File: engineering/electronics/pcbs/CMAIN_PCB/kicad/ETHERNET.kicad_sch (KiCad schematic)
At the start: 8 parts, among them J47 GIGABLOX_NANO_SWITCH_REVA_MOD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, J48 SM04B-GHS-TB_LF__SN_, J51 GIGABLOX_NANO_SWITCH_REVA_MOD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, J52 SM04B-GHS-TB_LF__SN_, U13 SMTWEM245STR, U14 SMTWEM245STR, U15 SMTWEM245STR, U16 SMTWEM245STR

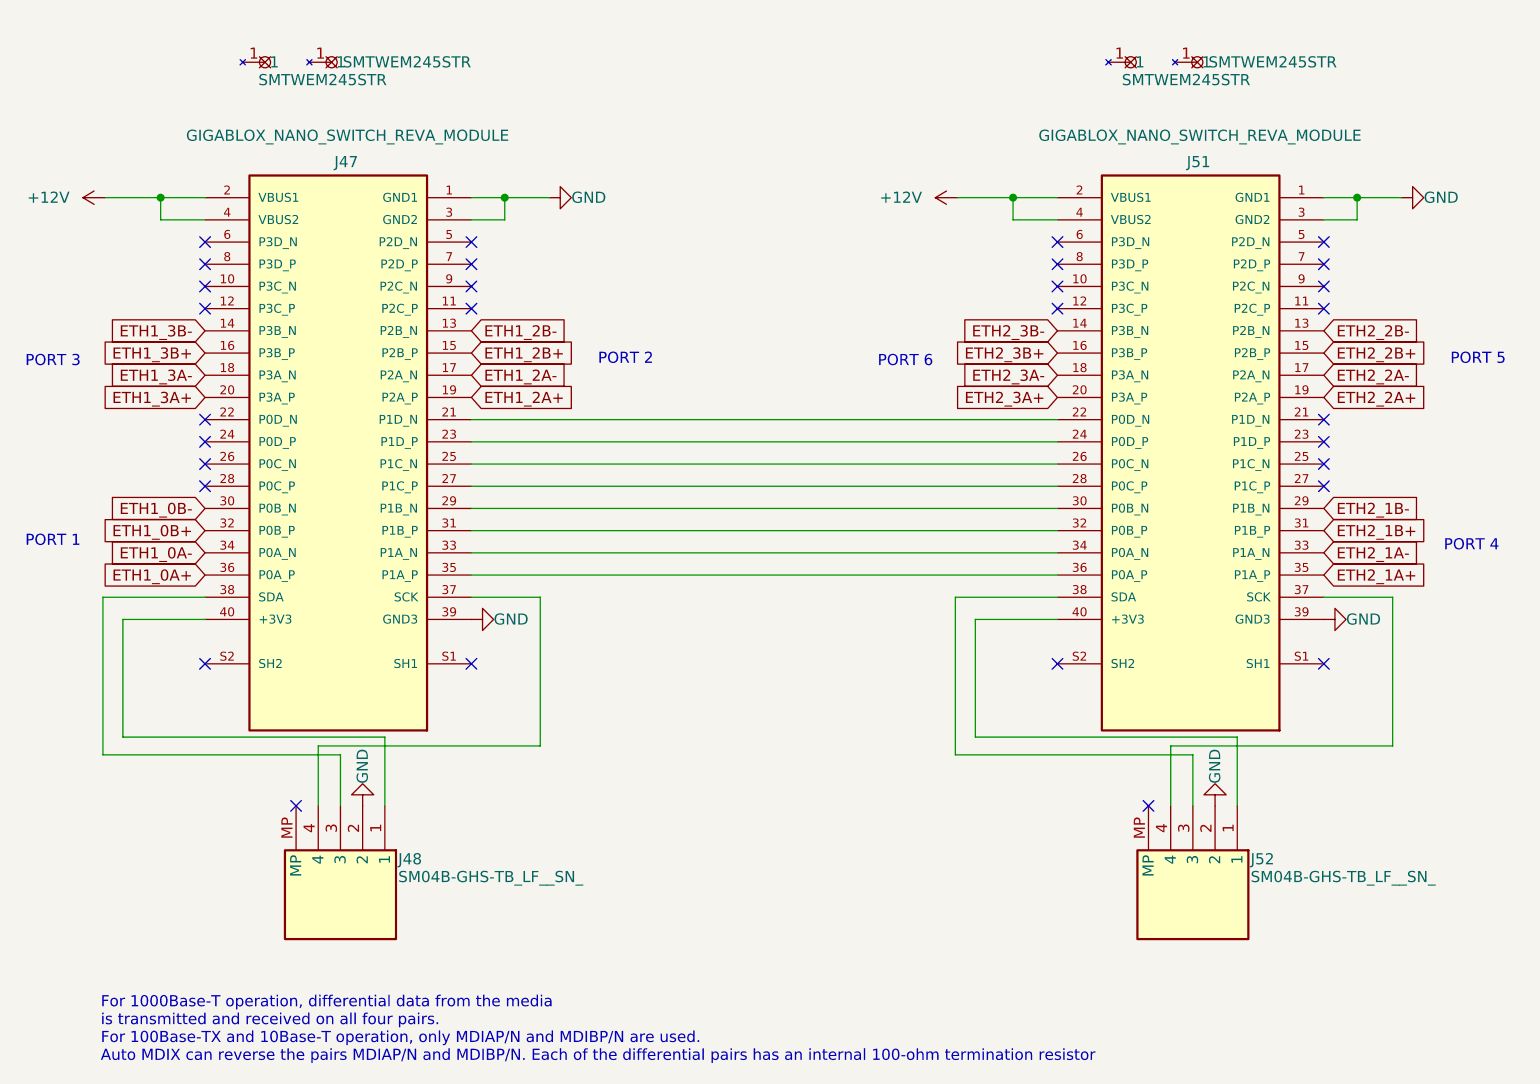
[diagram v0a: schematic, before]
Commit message: Import linked CMAIN PCB layout
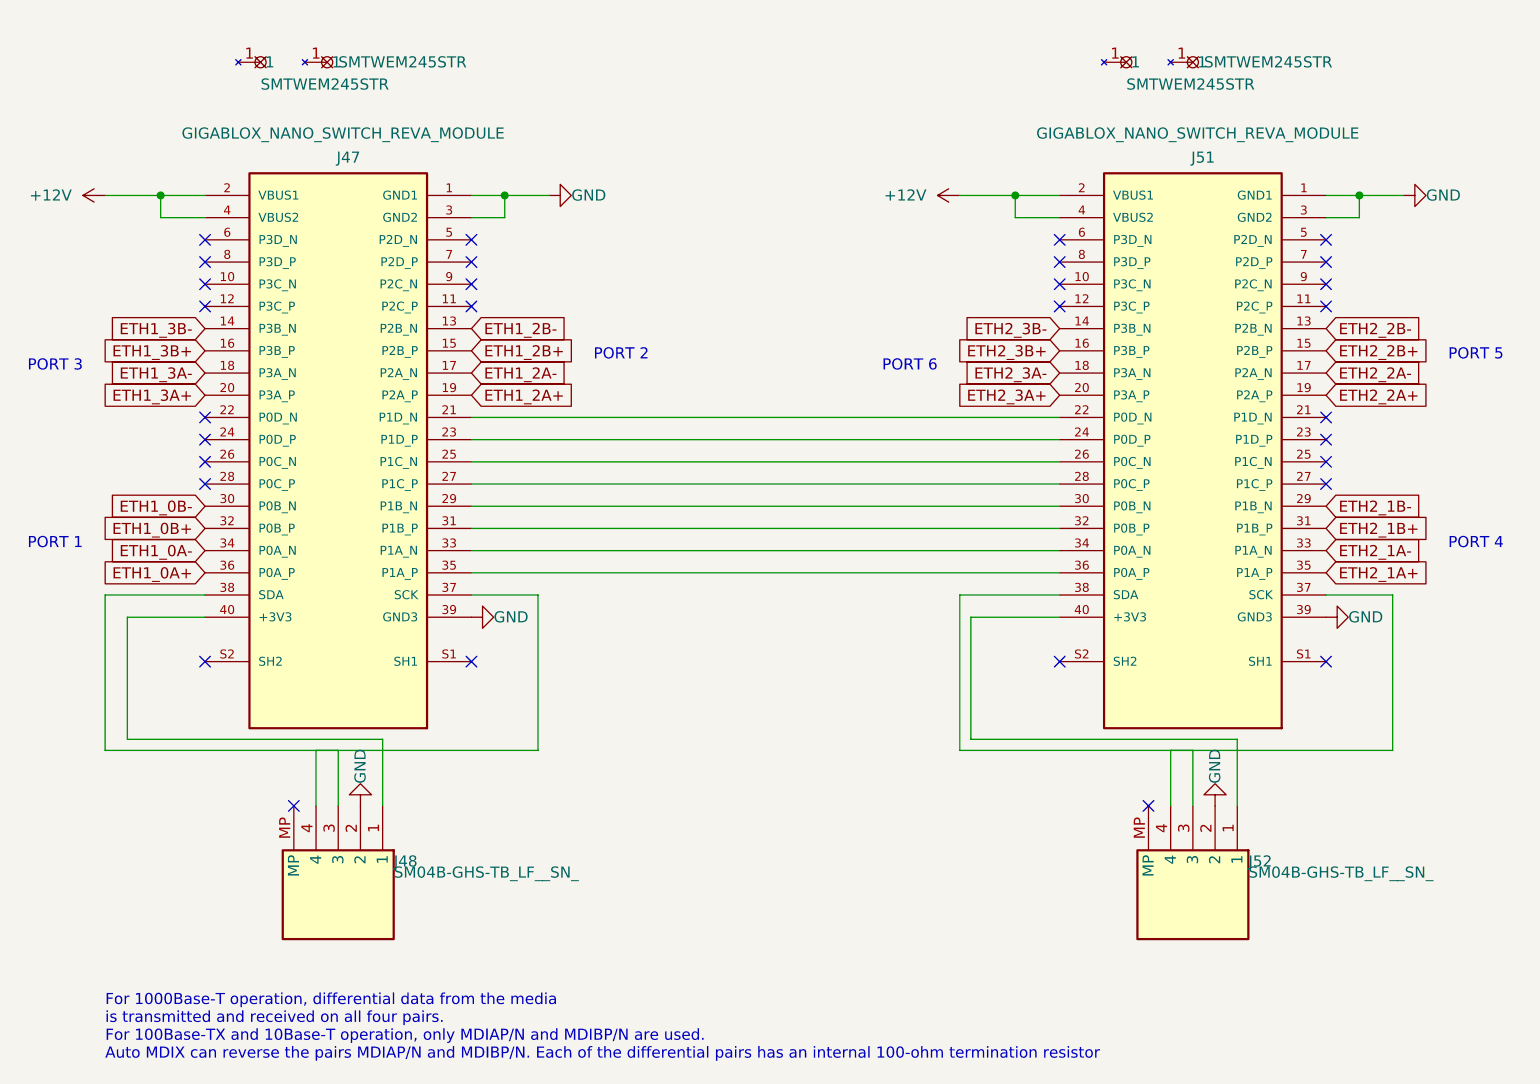
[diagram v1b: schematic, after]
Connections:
- net at J51.37 (SCK), J52.4: now also J51.38 (SDA), J52.3
- net at J47.37 (SCK), J48.4: now also J47.38 (SDA), J48.3

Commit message: electronics: update CMAIN and CBC PCB files
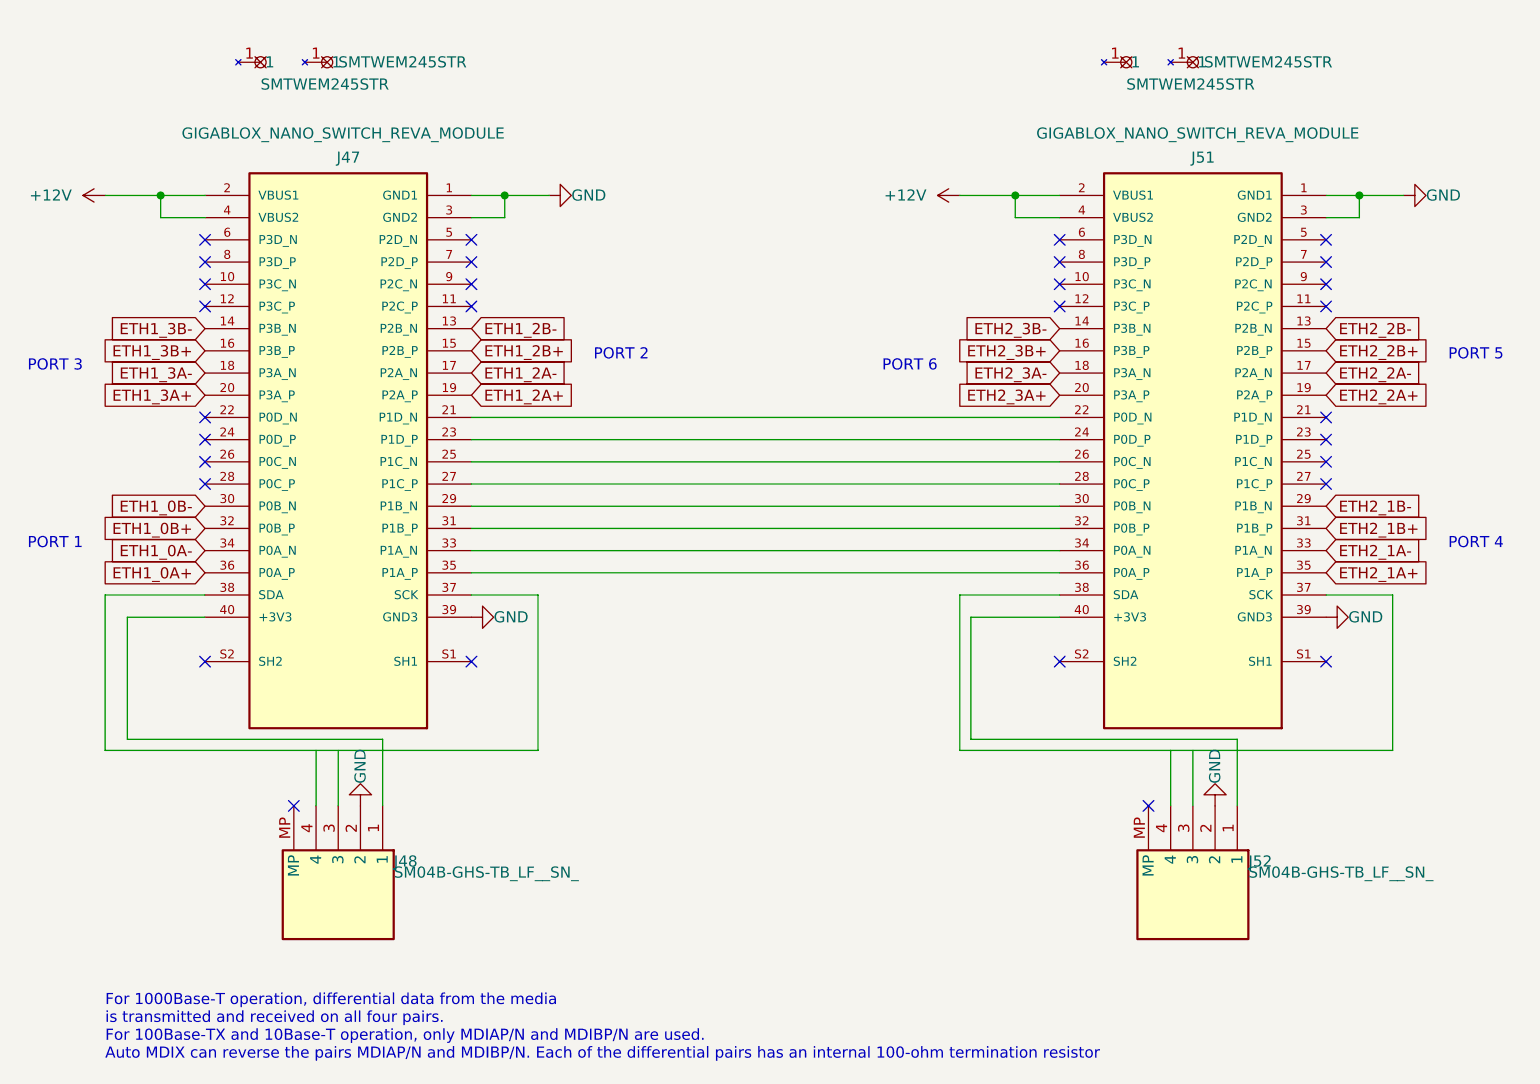
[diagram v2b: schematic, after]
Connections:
- net at J51.37 (SCK), J51.38 (SDA): no longer J52.3, J52.4
- net at J47.37 (SCK), J47.38 (SDA): no longer J48.3, J48.4
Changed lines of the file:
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@@
 	(wire
 		(pts
-			(xy 204.47 114.3) (xy 177.8 114.3)
+			(xy 177.8 114.3) (xy 227.33 114.3)
 		)
 		(stroke
@@
 	(wire
 		(pts
-			(xy 106.68 114.3) (xy 80.01 114.3)
+			(xy 80.01 114.3) (xy 129.54 114.3)
 		)
 		(stroke
@@
 	(wire
 		(pts
-			(xy 104.14 114.3) (xy 129.54 114.3)
-		)
-		(stroke
-			(width 0)
-			(type default)
-		)
-	)
-	(wire
-		(pts
 			(xy 129.54 96.52) (xy 121.92 96.52)
 		)
 		(stroke
-			(width 0)
-			(type default)
-		)
-	)
-	(wire
-		(pts
-			(xy 201.93 114.3) (xy 227.33 114.3)
-		)
-		(stroke

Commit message: electronics: clean up CMAIN local libraries
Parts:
- J48, J52: footprint Samacsys:SM04B-GHS-TB -> CMAIN_PCB:SM04B-GHS-TB
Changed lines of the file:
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@@
 			)
 		)
-		(property "Footprint" "Samacsys:SM04B-GHS-TB"
+		(property "Footprint" "CMAIN_PCB:SM04B-GHS-TB"
 			(at 114.3 137.16 0)
 			(hide yes)
@@
 			)
 		)
-		(property "Footprint" "Samacsys:SM04B-GHS-TB"
+		(property "Footprint" "CMAIN_PCB:SM04B-GHS-TB"
 			(at 16.51 137.16 0)
 			(hide yes)

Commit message: electronics: update CMAIN PCB from June layout
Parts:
- removed J48, J52: SM04B-GHS-TB_LF__SN_, CMAIN_PCB:SM04B-GHS-TB, symbol Samacsys_kicad_sym:SM04B-GHS-TB_LF__SN_
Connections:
- net at J51.37 (SCK): no longer J51.38 (SDA)
- net at J47.37 (SCK): no longer J47.38 (SDA)
- net +12V renamed 12V_1
- no-connect marks 30 -> 34

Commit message: electronics: shorten CMAIN footprint filenames for Windows
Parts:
- J47, J51: footprint Snapeda:GIGABLOX_NANO_SWITCH_REVA_MODULE_LSHM-120-02.5-L-DV-A-S-K-TR -> Snapeda:fp_072ec239da
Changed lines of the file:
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@@
 			)
 		)
-		(property "Footprint" "Snapeda:GIGABLOX_NANO_SWITCH_REVA_MODULE_LSHM-120-02.5-L-DV-A-S-K-TR"
+		(property "Footprint" "Snapeda:fp_072ec239da"
 			(at 214.63 111.76 0)
 			(hide yes)
@@
 			)
 		)
-		(property "Footprint" "Snapeda:GIGABLOX_NANO_SWITCH_REVA_MODULE_LSHM-120-02.5-L-DV-A-S-K-TR"
+		(property "Footprint" "Snapeda:fp_072ec239da"
 			(at 116.84 111.76 0)
 			(hide yes)

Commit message: electronics: integrate CMAIN STEP updates and consolidate footprints
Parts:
- J47, J51: footprint Snapeda:fp_072ec239da -> CMAIN_PCB:fp_072ec239da
- U13, U14, U15, U16: footprint Snapeda:SCREW-SMD_BD4.4-D2.8-H4.5 -> CMAIN_PCB:SCREW-SMD_BD4.4-D2.8-H4.5
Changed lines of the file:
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@@
 			)
 		)
-		(property "Footprint" "Snapeda:SCREW-SMD_BD4.4-D2.8-H4.5"
+		(property "Footprint" "CMAIN_PCB:SCREW-SMD_BD4.4-D2.8-H4.5"
 			(at 105.41 40.64 0)
 			(hide yes)
@@
 			)
 		)
-		(property "Footprint" "Snapeda:fp_072ec239da"
+		(property "Footprint" "CMAIN_PCB:fp_072ec239da"
 			(at 214.63 111.76 0)
 			(hide yes)
@@
 			)
 		)
-		(property "Footprint" "Snapeda:SCREW-SMD_BD4.4-D2.8-H4.5"
+		(property "Footprint" "CMAIN_PCB:SCREW-SMD_BD4.4-D2.8-H4.5"
 			(at 204.47 40.64 0)
 			(hide yes)
@@
 			)
 		)
-		(property "Footprint" "Snapeda:SCREW-SMD_BD4.4-D2.8-H4.5"
+		(property "Footprint" "CMAIN_PCB:SCREW-SMD_BD4.4-D2.8-H4.5"
 			(at 196.85 40.64 0)
 			(hide yes)
@@
 			)
 		)
-		(property "Footprint" "Snapeda:fp_072ec239da"
+		(property "Footprint" "CMAIN_PCB:fp_072ec239da"
 			(at 116.84 111.76 0)
 			(hide yes)
@@
 			)
 		)
-		(property "Footprint" "Snapeda:SCREW-SMD_BD4.4-D2.8-H4.5"
+		(property "Footprint" "CMAIN_PCB:SCREW-SMD_BD4.4-D2.8-H4.5"
 			(at 97.79 40.64 0)
 			(hide yes)

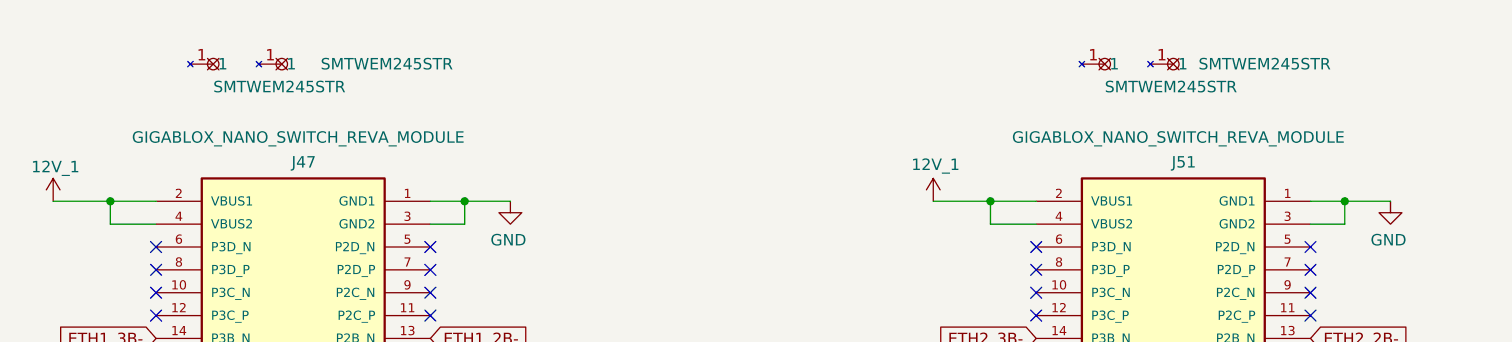
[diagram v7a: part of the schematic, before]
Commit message: fix(cmain): import KiCad updates with native libs
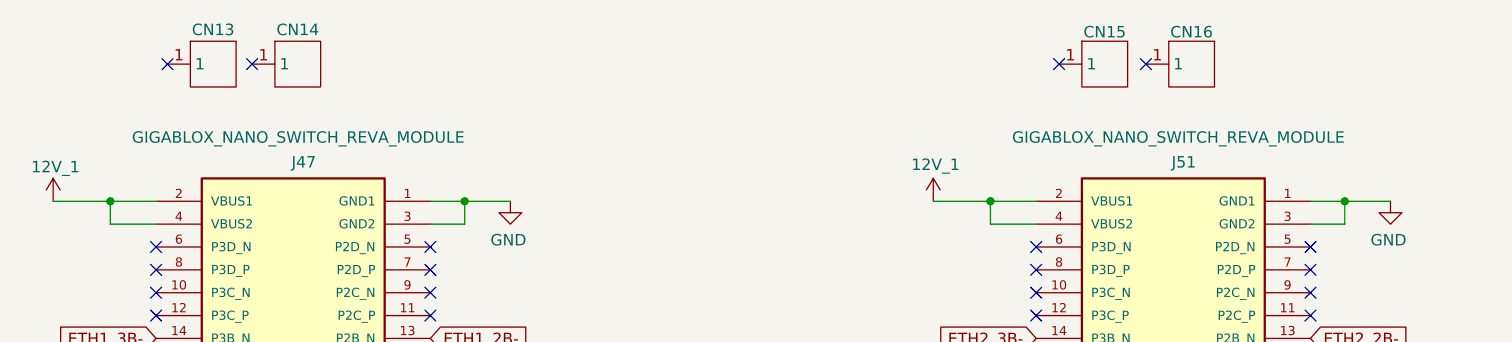
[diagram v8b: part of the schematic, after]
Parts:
- CN13: renamed from U13; value SMTWEM245STR -> (none); footprint CMAIN_PCB:SCREW-SMD_BD4.4-D2.8-H4.5 -> CMAIN_PCB:SCREW-SMD_TH162050CTJ; symbol Snapeda:SMTWEM245STR -> CMAIN_PCB:TH162050CTJ; LCSC Part Name YIYUAN(怡远) 电路板表贴圆螺母柱 PCB贴片连接器 M2x4.35xL4.5+1.4mm 铁镀锡 SMTWEM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 -> 雄和远景，电路板表贴圆螺母柱，M2Xφ4X5+1.5，铜镀锡，编带装; Manufacturer YIYUAN(怡远) -> Sinhoo(雄和远景); Manufacturer Part SMTWEM245STR -> TH162050CTJ; Supplier Part C5301792 -> C3020130
- CN14: renamed from U14; value SMTWEM245STR -> (none); footprint CMAIN_PCB:SCREW-SMD_BD4.4-D2.8-H4.5 -> CMAIN_PCB:SCREW-SMD_TH162050CTJ; symbol Snapeda:SMTWEM245STR -> CMAIN_PCB:TH162050CTJ; LCSC Part Name YIYUAN(怡远) 电路板表贴圆螺母柱 PCB贴片连接器 M2x4.35xL4.5+1.4mm 铁镀锡 SMTWEM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 -> 雄和远景，电路板表贴圆螺母柱，M2Xφ4X5+1.5，铜镀锡，编带装; Manufacturer YIYUAN(怡远) -> Sinhoo(雄和远景); Manufacturer Part SMTWEM245STR -> TH162050CTJ; Supplier Part C5301792 -> C3020130
- CN15: renamed from U15; value SMTWEM245STR -> (none); footprint CMAIN_PCB:SCREW-SMD_BD4.4-D2.8-H4.5 -> CMAIN_PCB:SCREW-SMD_TH162050CTJ; symbol Snapeda:SMTWEM245STR -> CMAIN_PCB:TH162050CTJ; LCSC Part Name YIYUAN(怡远) 电路板表贴圆螺母柱 PCB贴片连接器 M2x4.35xL4.5+1.4mm 铁镀锡 SMTWEM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 -> 雄和远景，电路板表贴圆螺母柱，M2Xφ4X5+1.5，铜镀锡，编带装; Manufacturer YIYUAN(怡远) -> Sinhoo(雄和远景); Manufacturer Part SMTWEM245STR -> TH162050CTJ; Supplier Part C5301792 -> C3020130
- CN16: renamed from U16; value SMTWEM245STR -> (none); footprint CMAIN_PCB:SCREW-SMD_BD4.4-D2.8-H4.5 -> CMAIN_PCB:SCREW-SMD_TH162050CTJ; symbol Snapeda:SMTWEM245STR -> CMAIN_PCB:TH162050CTJ; LCSC Part Name YIYUAN(怡远) 电路板表贴圆螺母柱 PCB贴片连接器 M2x4.35xL4.5+1.4mm 铁镀锡 SMTWEM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 -> 雄和远景，电路板表贴圆螺母柱，M2Xφ4X5+1.5，铜镀锡，编带装; Manufacturer YIYUAN(怡远) -> Sinhoo(雄和远景); Manufacturer Part SMTWEM245STR -> TH162050CTJ; Supplier Part C5301792 -> C3020130
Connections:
- no-connect marks 34 -> 38
